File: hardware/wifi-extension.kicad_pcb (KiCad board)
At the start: 2 copper layers, 40 x 40 mm, 25 parts, among them J1 STACK-UP-HIGH, J2 STACK-DOWN, J3 STACK-UP-HIGH, J4 STACK-DOWN, P1 CONN_6, U1 M24C64, U2 ESP8266_WROOM02, U3 NX3L2467, U4 DRILL, U5 DRILL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

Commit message: prototype finished
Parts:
- added Fiducial_Mark: VAL**, kicad-libraries:Fiducial_Mark, F.Cu at (164.1, 123.0)
- added Fiducial_Mark: VAL**, kicad-libraries:Fiducial_Mark, F.Cu at (138.6, 127.5)
- added Fiducial_Mark: VAL**, kicad-libraries:Fiducial_Mark, F.Cu at (167.1, 96.0)
- added Fiducial_Mark: VAL**, kicad-libraries:Fiducial_Mark, B.Cu at (167.1, 96.0)
- added Fiducial_Mark: VAL**, kicad-libraries:Fiducial_Mark, B.Cu at (163.6, 127.0)
- added Fiducial_Mark: VAL**, kicad-libraries:Fiducial_Mark, B.Cu at (138.6, 127.5)
- added VAL: WEEE_7mm_back, kicad-libraries:WEEE_7mm_back, B.Cu at (142.4, 117.6)
- added VAL: CE_5mm, kicad-libraries:CE_5mm, B.Cu at (157.6, 116.2)
- moved C2 5.27 mm to (139.0, 97.9), turned to 270 degrees
- moved C3 5.07 mm to (137.0, 97.7), turned to 270 degrees
- moved U2 5.00 mm to (151.1, 102.5)
- moved C4 3.81 mm to (134.5, 97.3), turned to 90 degrees
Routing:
- net GND: track 19.4 -> 68.9 mm, vias 14 -> 37
- net Net-(J3-Pad1): track 0.00 -> 29.2 mm, vias 0 -> 10
- net Net-(J3-Pad10): track 0.00 -> 29.2 mm, vias 0 -> 10
- net 3V3: track 99.9 -> 120.9 mm, vias 2 -> 3
- net Net-(J3-Pad22): track 0.00 -> 9.92 mm, vias 0 -> 3
- net SDA_ESP: track 13.7 -> 7.00 mm
- net FLASH_RX: track 19.2 -> 24.3 mm
- net EN: track 61.5 -> 66.4 mm
- net FLASH_TX: track 17.8 -> 22.5 mm
- net IO0: track 18.5 -> 23.3 mm
- net SCL_ESP: track 3.60 -> 7.41 mm
- net DATA_RX: track 18.0 -> 21.4 mm
- net Net-(J1-Pad14): track 0.00 -> 3.10 mm, vias 0 -> 1
- net Net-(J1-Pad10): track 0.00 -> 3.10 mm, vias 0 -> 1
- net Net-(J1-Pad6): track 0.00 -> 3.10 mm, vias 0 -> 1
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- added copper zone on B.Cu, net GND
- added copper zone on F.Cu, net GND

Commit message: change rx/tx interface to extension SPI interface
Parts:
- P1: footprint PIN_ARRAY_5x1 -> kicad-libraries:pin_array_6x1
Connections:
- net SCK renamed Net-(J1-Pad17)
- J1 pad 13: MISO -> RX
- J1 pad 15: MOSI -> TX
- J1 pad 26: RX -> Net-(J1-Pad26)
- J1 pad 28: TX -> Net-(J1-Pad28)
- J2 pad 13: MISO -> RX
- J2 pad 15: MOSI -> TX
- J2 pad 26: RX -> Net-(J1-Pad26)
- J2 pad 28: TX -> Net-(J1-Pad28)
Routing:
- net TX: track 18.4 -> 27.8 mm
- net GND: track 68.9 -> 77.7 mm, vias 37 -> 38
- net RX: track 17.5 -> 24.9 mm
- net 3V3: track 120.9 -> 126.3 mm
- net MOSI: track 2.90 -> 0.00 mm, vias 1 -> 0
- net Net-(J1-Pad28): track 0.00 -> 2.24 mm, vias 0 -> 1
- net Net-(J1-Pad26): track 0.00 -> 2.24 mm, vias 0 -> 1
- net MISO: track 2.20 -> 0.00 mm, vias 1 -> 0
- net IO0: track 23.3 -> 25.1 mm
- net LED: track 34.5 -> 34.0 mm
- net FLASH_TX: track 22.5 -> 23.0 mm

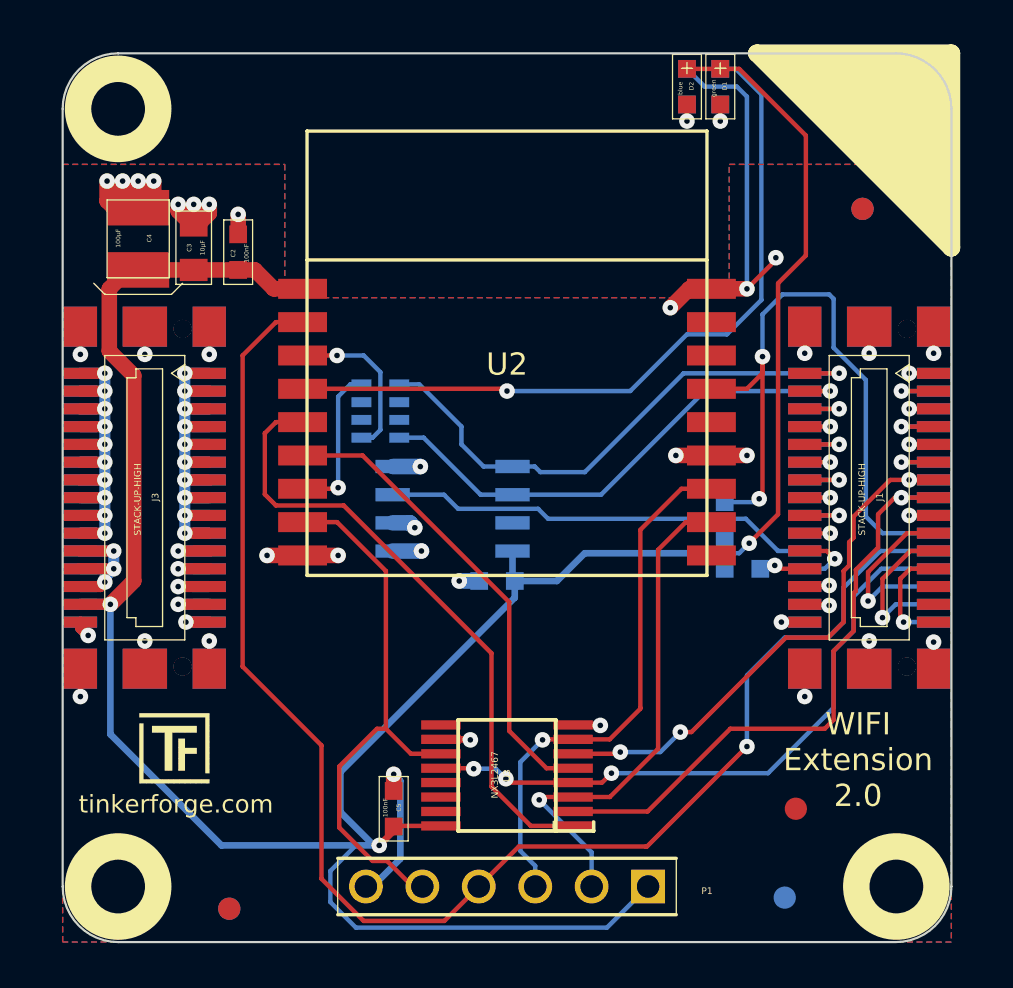
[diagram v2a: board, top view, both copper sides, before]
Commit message: fix flash interface
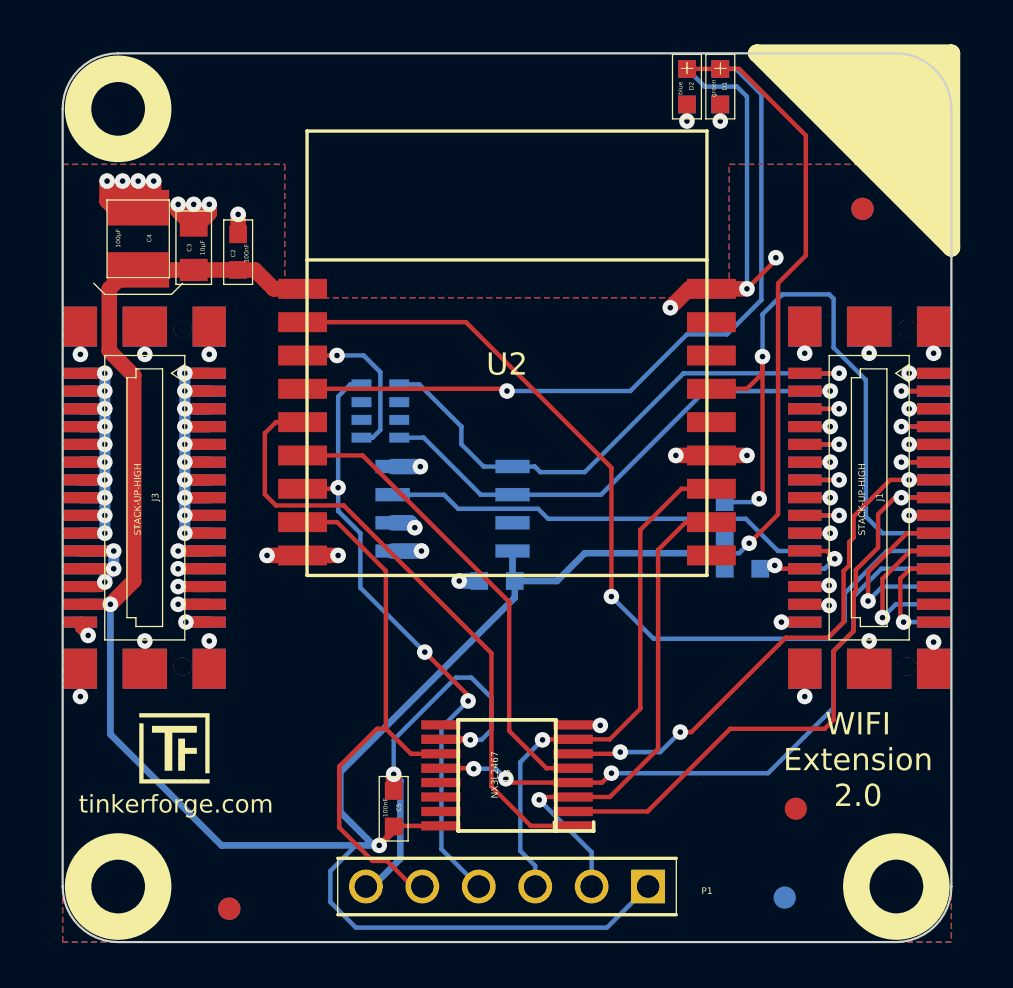
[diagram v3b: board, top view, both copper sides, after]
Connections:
- P1 pad 4: EN -> SDA_ESP
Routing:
- net EN: track 66.4 -> 40.1 mm
- net SDA_ESP: track 7.00 -> 28.6 mm, vias 1 -> 3
- net GND: track 77.7 -> 87.8 mm

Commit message: remove signal switch, new esp8266 signal connections
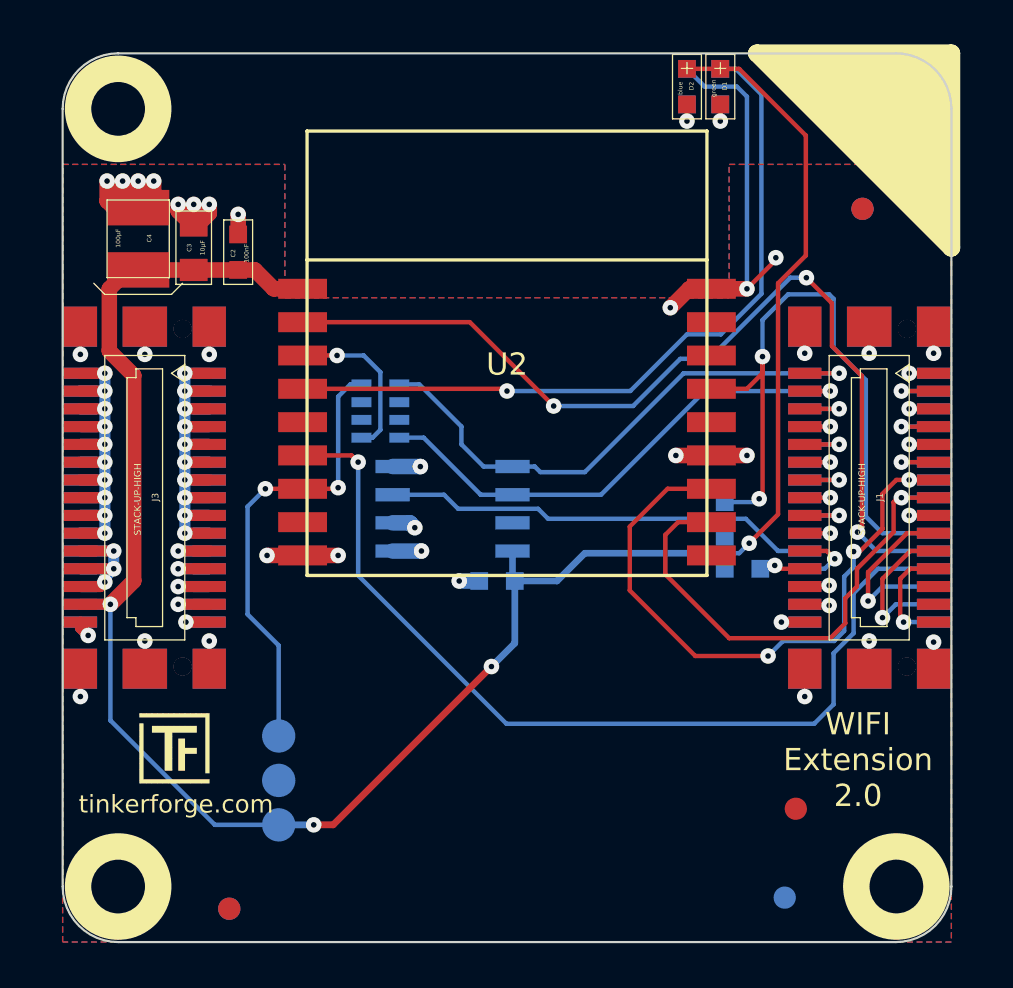
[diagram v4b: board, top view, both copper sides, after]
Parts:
- removed C5: 100nF, kicad-libraries:0603
- removed U7: DRILL, kicad-libraries:DRILL_NP
- added P2: CONN_1, kicad-libraries:TSTPT, B.Cu at (140.8, 119.7)
- added P3: CONN_1, kicad-libraries:TSTPT, B.Cu at (140.8, 121.7)
- P1: value CONN_6 -> CONN_1; footprint kicad-libraries:pin_array_6x1 -> kicad-libraries:TSTPT; moved to B.Cu
- U3: value NX3L2467 -> DRILL; footprint kicad-libraries:TSSOP16 -> kicad-libraries:DRILL_NP
- moved U3 18.2 mm to (168.6, 126.5), turned to 0 degrees
- moved P1 10.6 mm to (140.8, 123.7), turned to 0 degrees
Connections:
- J2 pad 23: FLASH_CTRL -> GP
- U2 pad 11: FLASH_TX -> TX
- U2 pad 12: FLASH_RX -> RX
- U2 pad 5: DATA_TX -> (no net)
- U2 pad 6: DATA_RX -> GP
- U2 pad 8: IO0 -> (no net)
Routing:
- net GP: track 0.00 -> 41.7 mm, vias 0 -> 1
- net FLASH_CTRL: track 28.8 -> 0.00 mm, vias 3 -> 0
- net DATA_TX: track 28.2 -> 0.00 mm
- net 3V3: track 126.3 -> 98.9 mm, vias 3 -> 4
- net IO0: track 25.1 -> 0.00 mm
- net FLASH_RX: track 24.3 -> 0.00 mm, vias 1 -> 0
- net FLASH_TX: track 23.0 -> 0.00 mm, vias 1 -> 0
- net DATA_RX: track 21.4 -> 0.00 mm
- net GND: track 87.8 -> 67.5 mm, vias 38 -> 35
- net SDA_ESP: track 28.6 -> 20.7 mm, vias 3 -> 2
- net TX: track 27.8 -> 23.3 mm
- net RX: track 24.9 -> 29.3 mm
- net EN: track 40.1 -> 43.0 mm, vias 1 -> 3

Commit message: fully routed
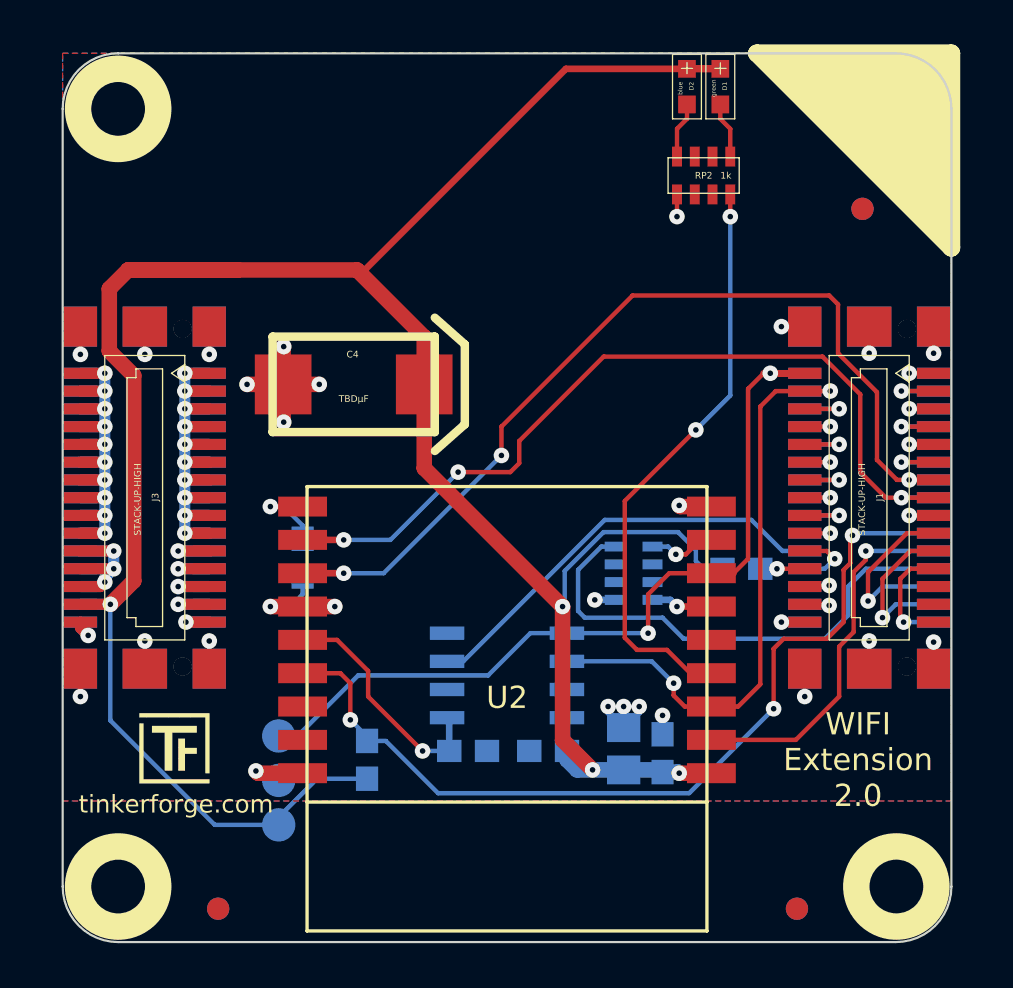
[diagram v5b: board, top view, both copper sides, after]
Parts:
- added RP2: 1k, kicad-libraries:0603X4, F.Cu at (159.9, 94.5)
- C1, R1, R2, R3, R4: footprint kicad-libraries:0603 -> kicad-libraries:0603E
- C2: footprint kicad-libraries:0603 -> kicad-libraries:0603E; moved to B.Cu
- C3: footprint kicad-libraries:0805 -> kicad-libraries:0805E; moved to B.Cu
- C4: value 100µF -> TBDµF; footprint kicad-libraries:3528-21 -> kicad-libraries:7343
- RP1: value 0 -> 1k
- moved R2 31.5 mm to (149.3, 120.3), turned to 0 degrees
- moved C3 29.7 mm to (156.3, 120.2)
- moved C2 29.6 mm to (158.1, 120.5)
- moved R1 28.3 mm to (141.9, 111.7), turned to 270 degrees
- moved R3 19.4 mm to (144.8, 120.8)
- moved U2 16.0 mm to (151.1, 118.5), turned to 180 degrees
- moved RP1 13.5 mm to (156.8, 112.3), turned to 270 degrees
- moved C4 11.7 mm to (144.2, 103.8), turned to 180 degrees
- moved C1 7.99 mm to (152.9, 120.3)
- moved U1 7.89 mm to (151.1, 117.0)
- moved Fiducial_Mark 4.50 mm to (164.1, 127.5)
- moved Fiducial_Mark 0.74 mm to (164.1, 127.5)
- moved Fiducial_Mark 0.50 mm to (138.1, 127.5) (x2)
- moved R4 0.05 mm to (161.6, 112.2)
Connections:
- J2 pad 23: GP -> IO0
- P2 pad 1: SDA_ESP -> SDA
- R1 pad 1: Net-(D1-Pad2) -> Net-(R1-Pad1)
- R1 pad 2: LED -> GND
- R2 pad 1: Net-(D2-Pad2) -> EEPROM_SEL
- RP1 pad 1: SDA -> GND
- RP1 pad 4: SCL -> IO0
- RP1 pad 5: SCL_ESP -> Net-(RP1-Pad5)
- RP1 pad 8: SDA_ESP -> Net-(RP1-Pad8)
- U1 pad 1: GND -> EEPROM_SEL
- U2 pad 10: (no net) -> Net-(R1-Pad1)
- U2 pad 14: (no net) -> EEPROM_SEL
- U2 pad 3: SCL_ESP -> SCL
- U2 pad 6: GP -> Net-(RP1-Pad8)
- U2 pad 7: SDA_ESP -> SDA
- U2 pad 8: (no net) -> Net-(RP1-Pad5)
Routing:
- net GP: track 41.7 -> 0.00 mm, vias 1 -> 0
- net EN: track 43.0 -> 17.6 mm, vias 3 -> 1
- net 3V3: track 98.9 -> 121.6 mm
- net IO0: track 0.00 -> 22.5 mm
- net SDA_ESP: track 20.7 -> 0.00 mm, vias 2 -> 0
- net GND: track 67.5 -> 51.2 mm, vias 35 -> 30
- net TX: track 23.3 -> 38.5 mm, vias 1 -> 3
- net SDA: track 25.3 -> 39.1 mm, vias 1 -> 2
- net RX: track 29.3 -> 42.0 mm
- net EEPROM_SEL: track 0.00 -> 10.9 mm, vias 0 -> 1
- net nRESET: track 30.6 -> 40.2 mm, vias 2 -> 3
- net SCL_ESP: track 7.41 -> 0.00 mm, vias 1 -> 0
- net LED: track 33.8 -> 26.5 mm, vias 1 -> 2
- net Net-(R1-Pad1): track 0.00 -> 3.85 mm, vias 0 -> 1
- net SCL: track 23.5 -> 27.4 mm, vias 1 -> 2
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
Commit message: ordered prototype
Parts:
- added G***: LOGO, kicad-libraries:TF_Wireless, F.Cu at (151.1, 99.5)

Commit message: remove antenna symbol, move ce and weee logo
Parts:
- removed the G*** at (151.1, 99.5)
- moved VAL 19.7 mm to (143.8, 98.0)
- moved VAL 18.2 mm to (158.4, 98.0)

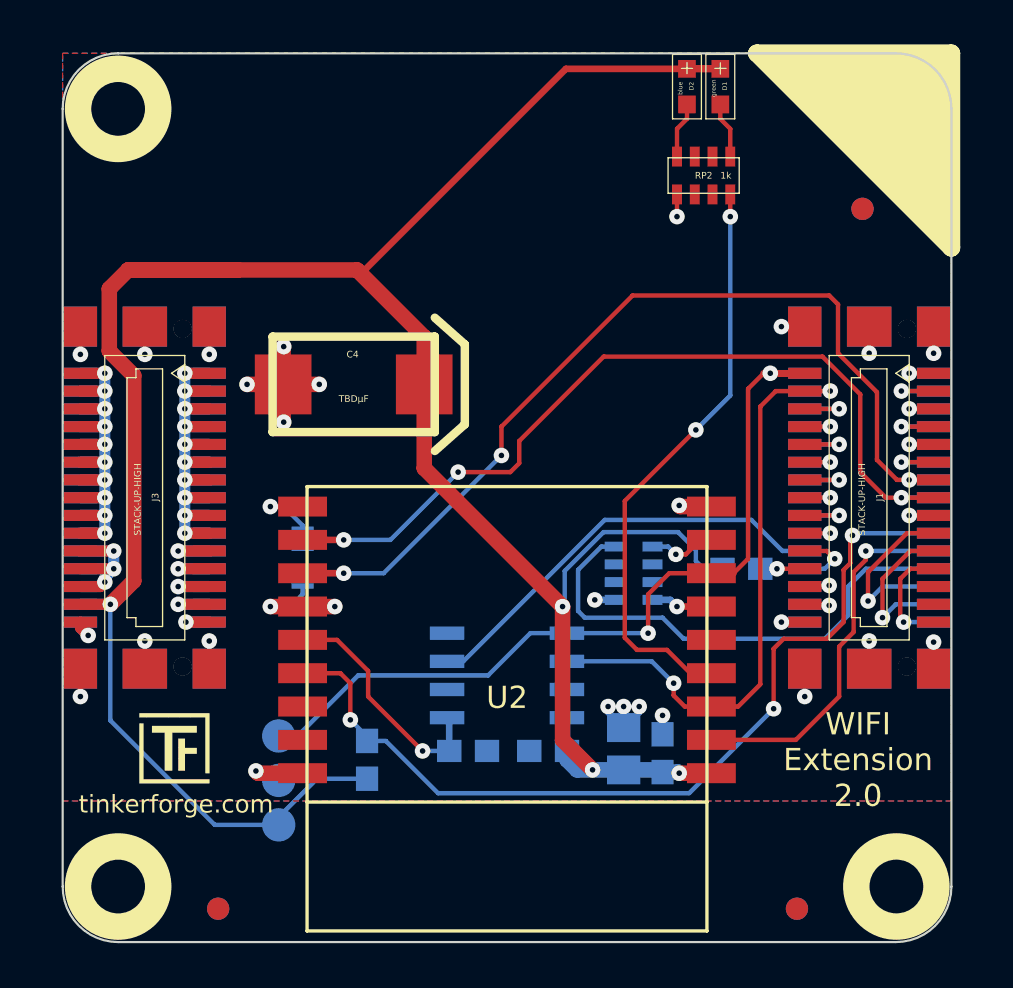
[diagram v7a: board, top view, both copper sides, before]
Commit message: add filter, change silkscreen
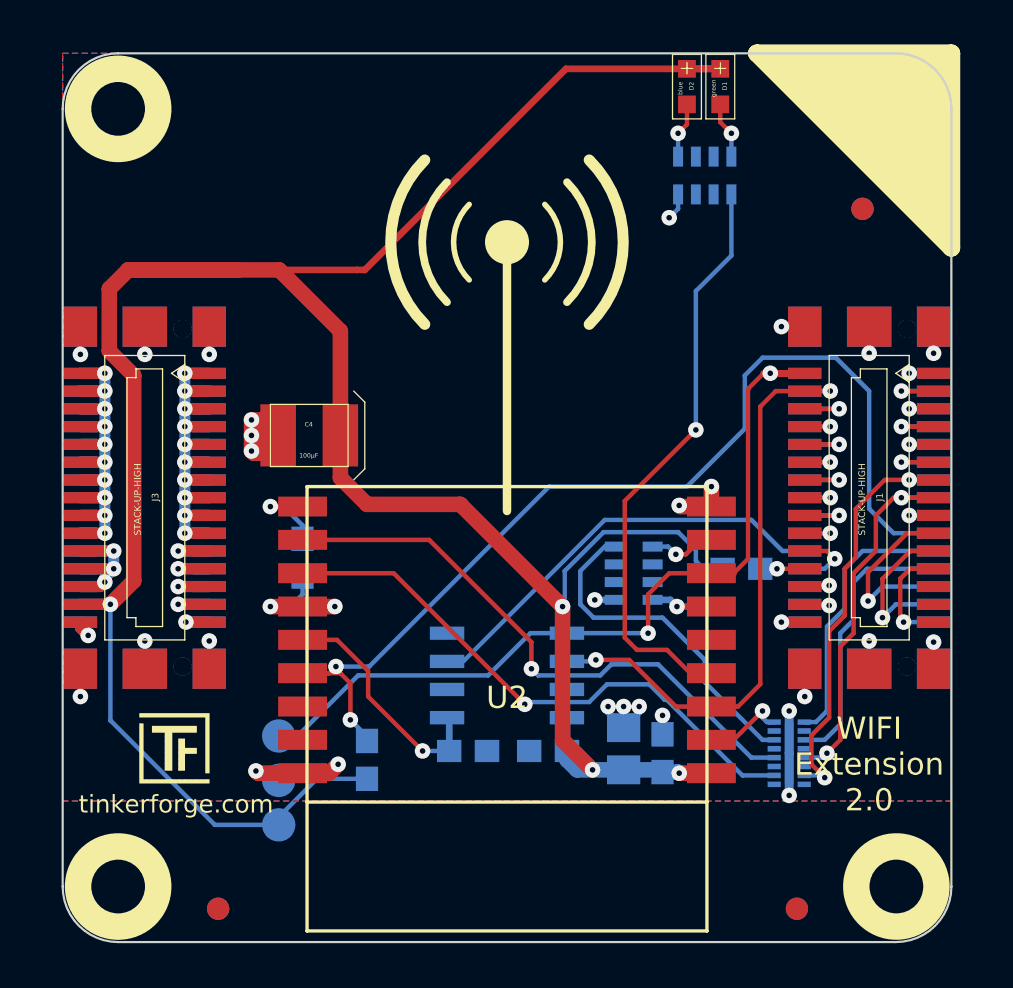
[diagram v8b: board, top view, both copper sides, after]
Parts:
- added FILTER1: Filter-8x, kicad-libraries:DFN16-33x135, B.Cu at (163.8, 120.5)
- C4: value TBDµF -> 100µF; footprint kicad-libraries:7343 -> kicad-libraries:3528-21
- RP2: moved to B.Cu
- moved C4 3.05 mm to (142.2, 106.2)
- turned RP2 to 180 degrees
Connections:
- RP1 pad 4: IO0 -> Net-(FILTER1-Pad14)
- RP2 pad 1: Net-(D1-Pad2) -> Net-(D2-Pad2)
- RP2 pad 4: Net-(D2-Pad2) -> Net-(D1-Pad2)
- RP2 pad 5: GND -> LED
- RP2 pad 8: LED -> GND
- U2 pad 11: TX -> Net-(FILTER1-Pad12)
- U2 pad 12: RX -> Net-(FILTER1-Pad10)
- U2 pad 2: EN -> Net-(FILTER1-Pad16)
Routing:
- net Net-(FILTER1-Pad12): track 0.00 -> 26.4 mm, vias 0 -> 1
- net Net-(FILTER1-Pad10): track 0.00 -> 25.7 mm, vias 0 -> 1
- net RX: track 42.0 -> 19.3 mm, vias 3 -> 2
- net TX: track 38.5 -> 17.1 mm, vias 3 -> 2
- net Net-(FILTER1-Pad14): track 0.00 -> 15.3 mm
- net 3V3: track 121.6 -> 132.3 mm
- net IO0: track 22.5 -> 12.4 mm
- net nRESET: track 40.2 -> 47.3 mm, vias 3 -> 2
- net GND: track 51.2 -> 56.9 mm, vias 30 -> 33
- net Net-(FILTER1-Pad16): track 0.00 -> 5.55 mm, vias 0 -> 1
- net EN: track 17.6 -> 12.3 mm, vias 1 -> 0
- net Net-(D1-Pad2): track 2.53 -> 2.56 mm, vias 0 -> 1
- net Net-(D2-Pad2): track 2.53 -> 2.52 mm, vias 0 -> 1
- net LED: vias 2 -> 1
